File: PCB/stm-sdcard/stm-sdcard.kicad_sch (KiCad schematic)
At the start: 28 parts, among them J1 Conn_01x04_Pin, J2 Conn_01x03_Pin, SW1 SW_Push, SW2 SW_Push, U4 TLV1117LV33DCYR

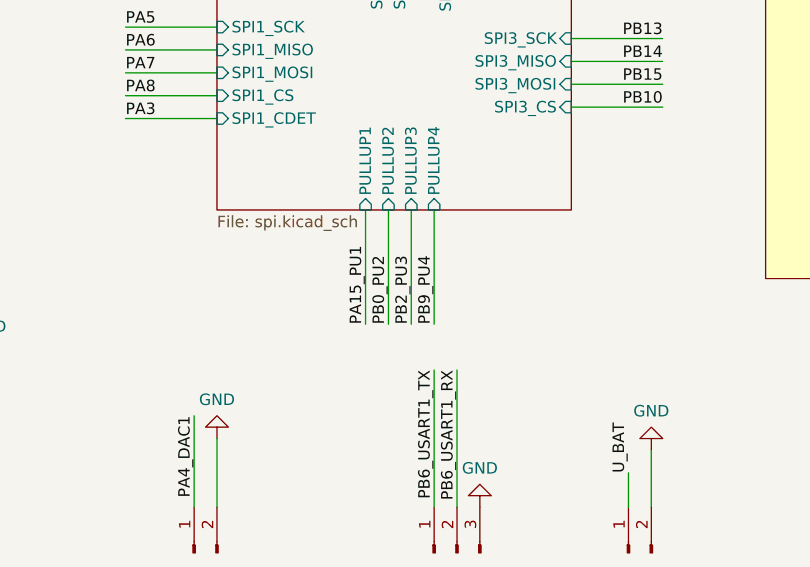
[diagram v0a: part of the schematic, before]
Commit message: Routing done, errors corrected
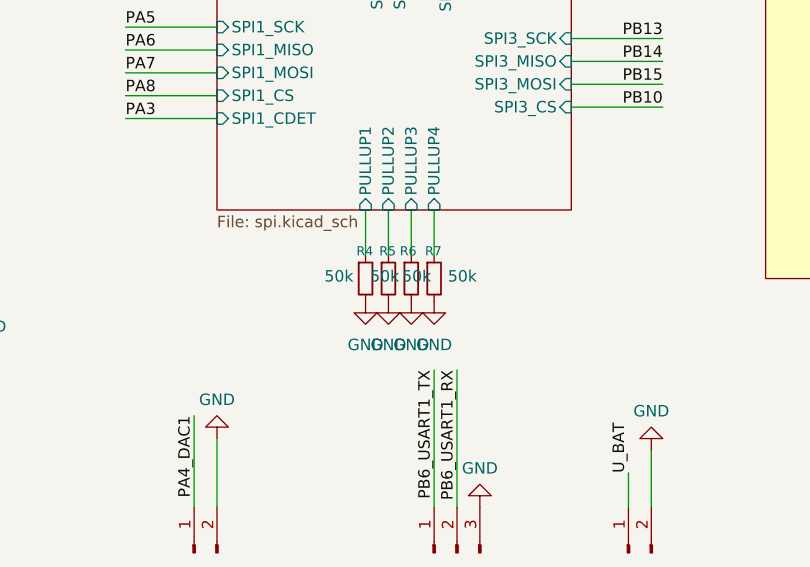
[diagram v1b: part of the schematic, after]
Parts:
- added R4, R5, R6, R7: 50k, Resistor_SMD:R_0805_2012Metric_Pad1.20x1.40mm_HandSolder, symbol Device:R_Small
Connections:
- net GND: now also R4.2, R5.2, R6.2, R7.2
- new net SPI-SDcard/PULLUP1: R4.1
- new net SPI-SDcard/PULLUP2: R5.1
- new net SPI-SDcard/PULLUP3: R6.1
- new net SPI-SDcard/PULLUP4: R7.1
